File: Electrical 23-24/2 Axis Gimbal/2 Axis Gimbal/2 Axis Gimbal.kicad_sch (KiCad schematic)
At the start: 25 parts, among them IC1 BNO085, J1 Conn_01x06_Socket, U1 ATtiny404-SS

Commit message: Fix some gimbal problems
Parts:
- added I2C, Power: Conn_01x02_Socket, symbol Connector:Conn_01x02_Socket
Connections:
- net +BATT: now also Power.1 (Pin_1)
- net GND: now also Power.2 (Pin_2)
- net MOSI: now also U1.11 (PA1); no longer U1.13 (PA3)
- net RX: now also U1.6 (PB3); no longer U1.7 (PB2)
- net SCK: now also U1.13 (PA3); no longer U1.11 (PA1)
- net TX: now also U1.7 (PB2); no longer U1.6 (PB3)
- net SDA: now reaches U1.8 (PB1)
- net SDA: now also I2C.1 (Pin_1)
- net SCL: now reaches U1.9 (PB0)
- net SCL: now also I2C.2 (Pin_2)
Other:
- note added: "I2C Breakout"
- note added: "Power"
- moved on the sheet: C2, C3, D-CUP, D-CUP1, D-CUP2, IC1, R1, R2, R3, R4, R5, R6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

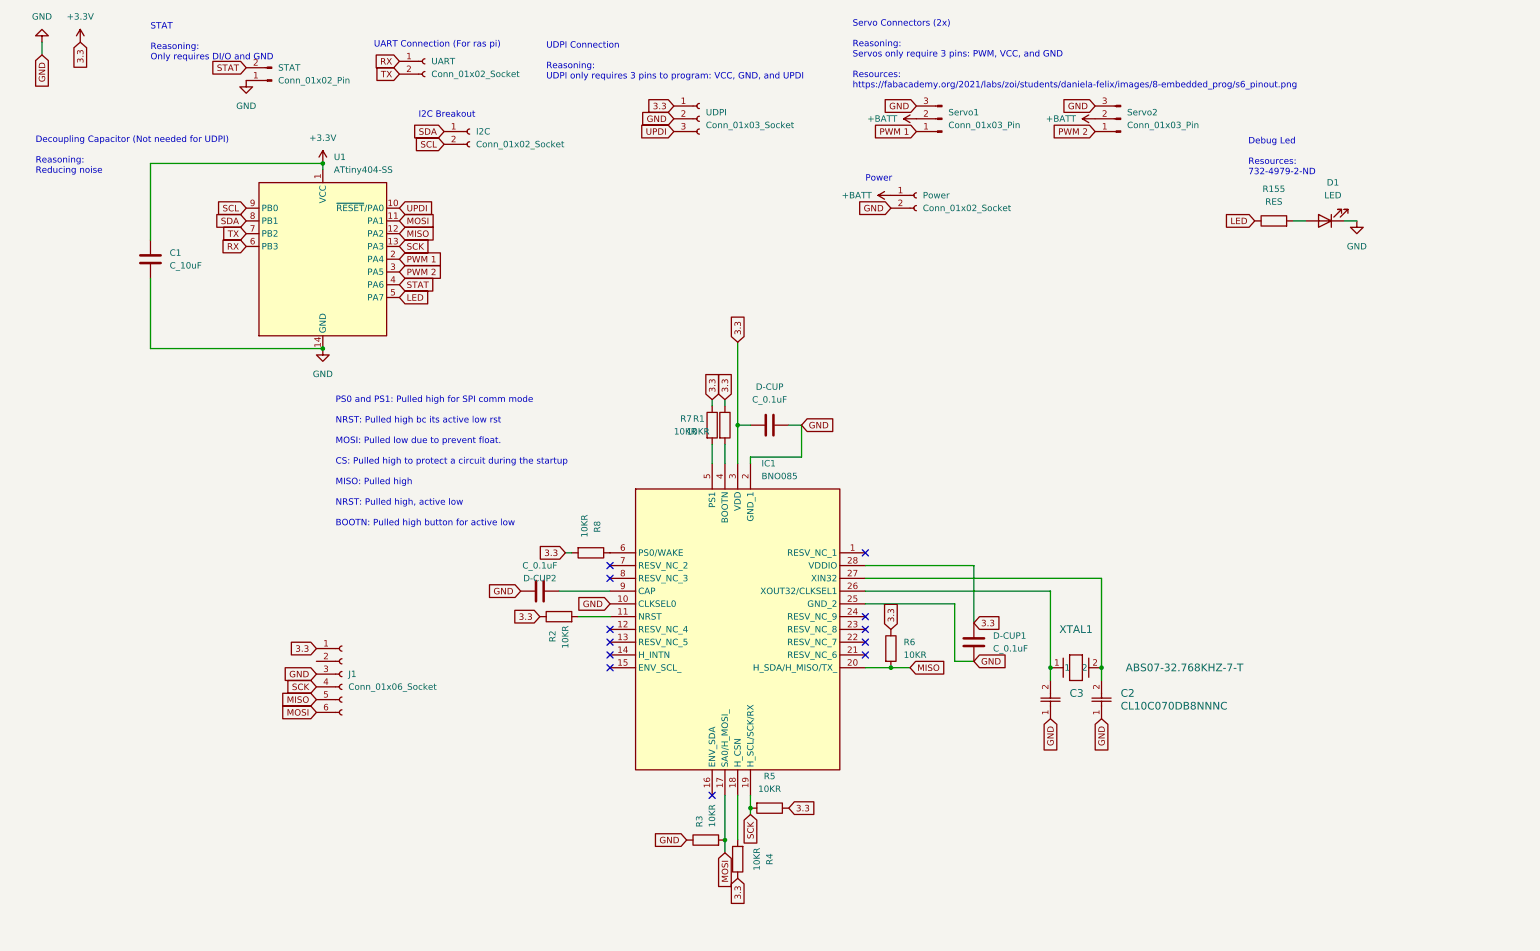
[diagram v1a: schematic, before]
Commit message: Added I2C
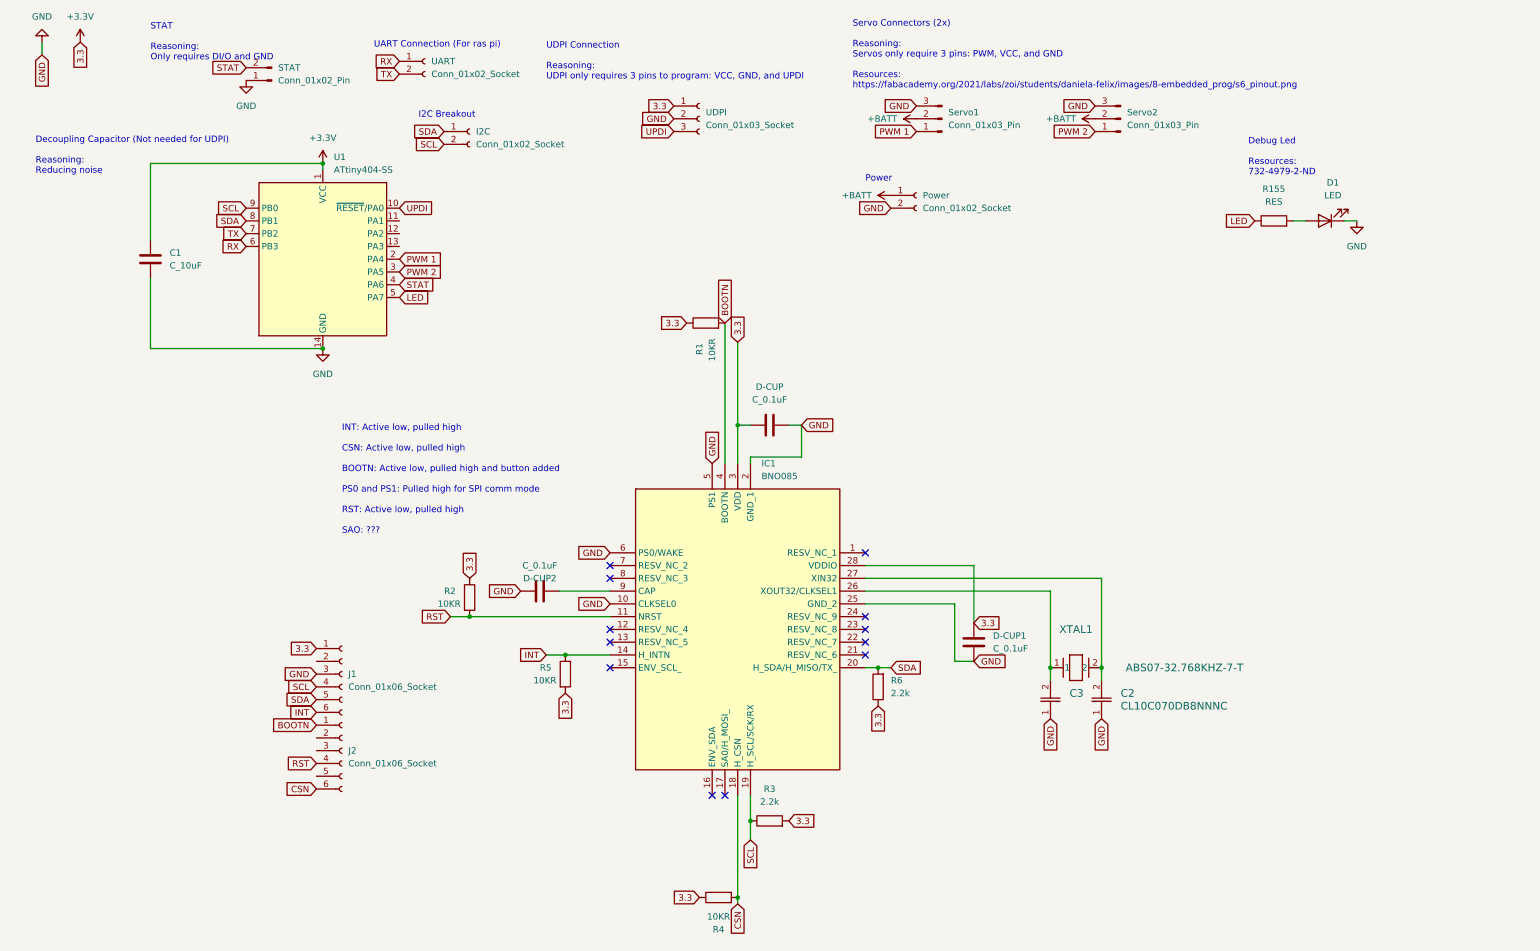
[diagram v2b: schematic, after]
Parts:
- removed R3, R6, R7, R8: 10KR, symbol oem:10KR
- added J2: Conn_01x06_Socket, symbol Connector:Conn_01x06_Socket
- added R3, R6: 2.2k, symbol Device:R
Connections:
- net +3.3V: now also R5.2, R3.2, R6.1; no longer R5.1
- net GND: now also IC1.5 (PS1), IC1.6 (PS0/WAKE)
- net SCL: now also IC1.19 (H_SCL/SCK/RX), J1.4 (Pin_4), R3.1
- net SDA: now also IC1.20 (H_SDA/H_MISO/TX_), J1.5 (Pin_5), R6.2
- net RST: now reaches IC1.11 (NRST), R2.2
- net RST: now also J2.4 (Pin_4)
- net INT: now reaches IC1.14 (H_INTN)
- net INT: now also J1.6 (Pin_6), R5.1
- net CSN: now reaches IC1.18 (H_CSN), R4.2
- net CSN: now also J2.6 (Pin_6)
- net BOOTN: now reaches IC1.4 (BOOTN), R1.2
- net BOOTN: now also J2.1 (Pin_1)
- removed net MISO: IC1.20 (H_SDA/H_MISO/TX_), J1.5 (Pin_5), U1.12 (PA2)
- removed net MOSI: IC1.17 (SA0/H_MOSI_), J1.6 (Pin_6), U1.11 (PA1)
- removed net SCK: IC1.19 (H_SCL/SCK/RX), J1.4 (Pin_4), R5.2, U1.13 (PA3)
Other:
- note added: "INT: Active low, pulled high CSN: Active low, pulled high BOOTN: Active low, pulled high and button added PS0 and PS1: Pulled high for SPI comm mode RST: Active low, pulled high SAO: ???"
- note removed: "PS0 and PS1: Pulled high for SPI comm mode NRST: Pulled high bc its active low rst MOSI: Pulled low due to prevent float. CS: Pulled high to protect a circuit during the startup MISO: Pulled high NRST: Pulled high, active low BOOTN: Pulled high button for active low"
- moved on the sheet: R1, R2, R4

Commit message: Finished Final Schematic
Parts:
- added C4, C5: C_100uF, Capacitor_SMD:C_1206_3216Metric_Pad1.33x1.80mm_HandSolder, symbol formula:C_100uF
- added IC2: AP1086DL-13, TO252-3L_1, symbol VReg3.3:AP1086DL-13
- C1: footprint footprints:C_0805_OEM -> Capacitor_SMD:C_0805_2012Metric_Pad1.18x1.45mm_HandSolder
- C2, C3: footprint CAP_CL10_SAM -> Capacitor_SMD:C_0201_0603Metric_Pad0.64x0.40mm_HandSolder
- D-CUP, D-CUP1, D-CUP2: footprint footprints:C_0805_OEM -> Capacitor_SMD:C_0402_1005Metric_Pad0.74x0.62mm_HandSolder
- D1: footprint (none) -> LED_SMD:LED_0603_1608Metric_Pad1.05x0.95mm_HandSolder
- I2C, Power, UART: footprint (none) -> Connector_PinSocket_2.54mm:PinSocket_1x02_P2.54mm_Vertical
- J1, J2: footprint (none) -> Connector_PinHeader_2.54mm:PinHeader_1x06_P2.54mm_Vertical
- R1: footprint (none) -> Resistor_SMD:R_0201_0603Metric_Pad0.64x0.40mm_HandSolder
- R2, R4, R5: footprint (none) -> Resistor_SMD:R_0603_1608Metric_Pad0.98x0.95mm_HandSolder
- R3, R6: footprint (none) -> Resistor_SMD:R_1206_3216Metric_Pad1.30x1.75mm_HandSolder
- R55: renamed from R155; footprint (none) -> LED_SMD:LED_1206_3216Metric_Pad1.42x1.75mm_HandSolder
- STAT: footprint (none) -> Connector_PinHeader_2.54mm:PinHeader_1x02_P2.54mm_Vertical
- Servo1, Servo2: footprint (none) -> Connector_PinHeader_2.54mm:PinHeader_1x03_P2.54mm_Vertical
- UDPI: footprint (none) -> Connector_PinSocket_2.54mm:PinSocket_1x03_P2.54mm_Vertical
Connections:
- net GND: now also C4.2, C5.2, IC2.1 (ADJ_(GND))
- net +3.3V renamed 3.3
- net 3.3: now also C4.1, IC2.3 (VOUT)
- new net +5V: C5.1, IC2.2 (VIN)
- no-connect marks 12 -> 19
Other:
- moved on the sheet: J1, J2

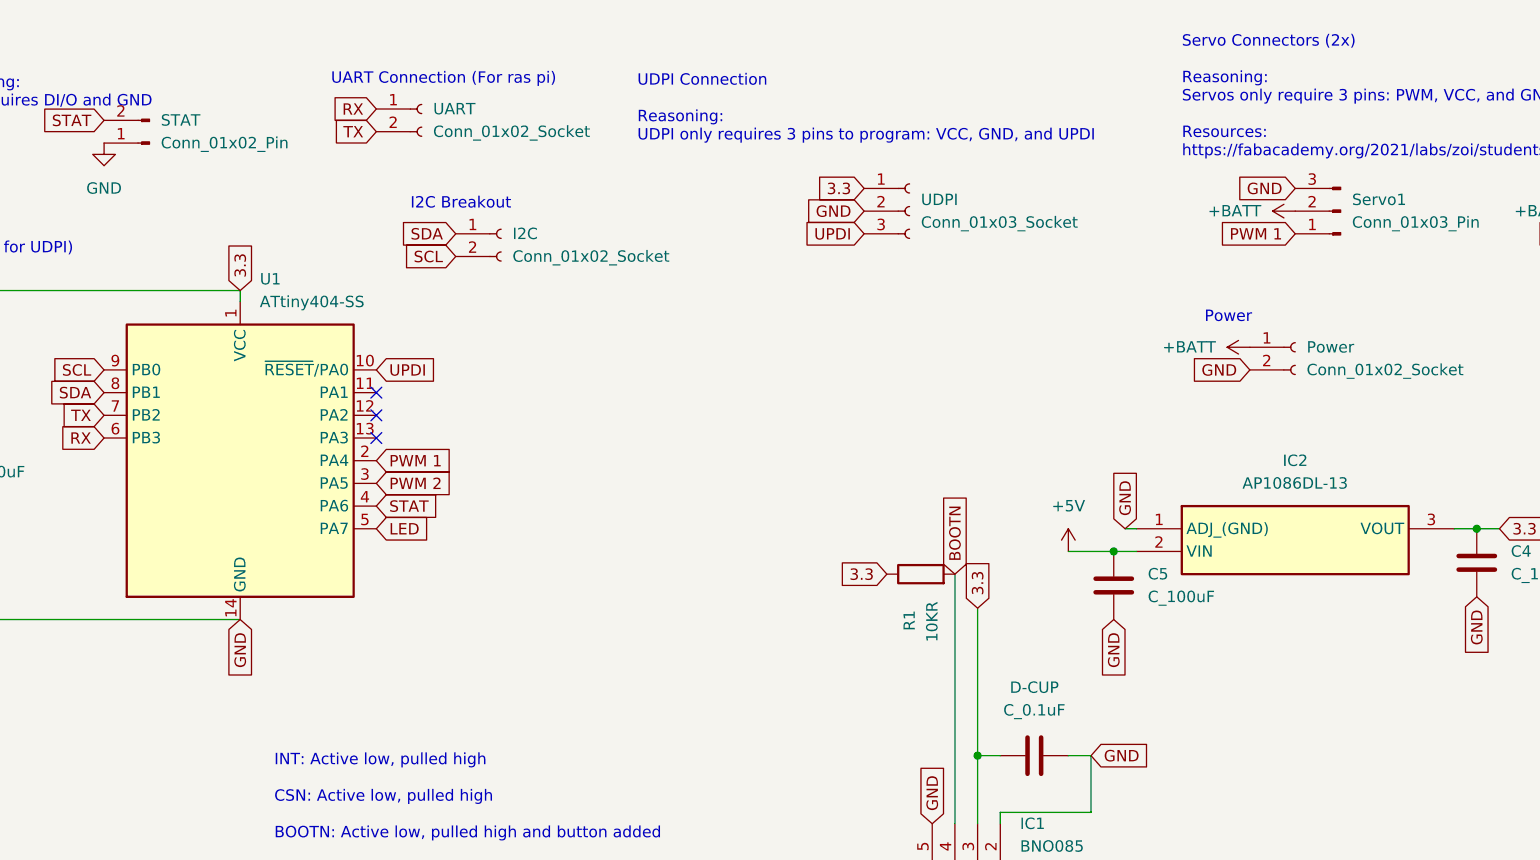
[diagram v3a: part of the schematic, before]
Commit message: Added Footprints
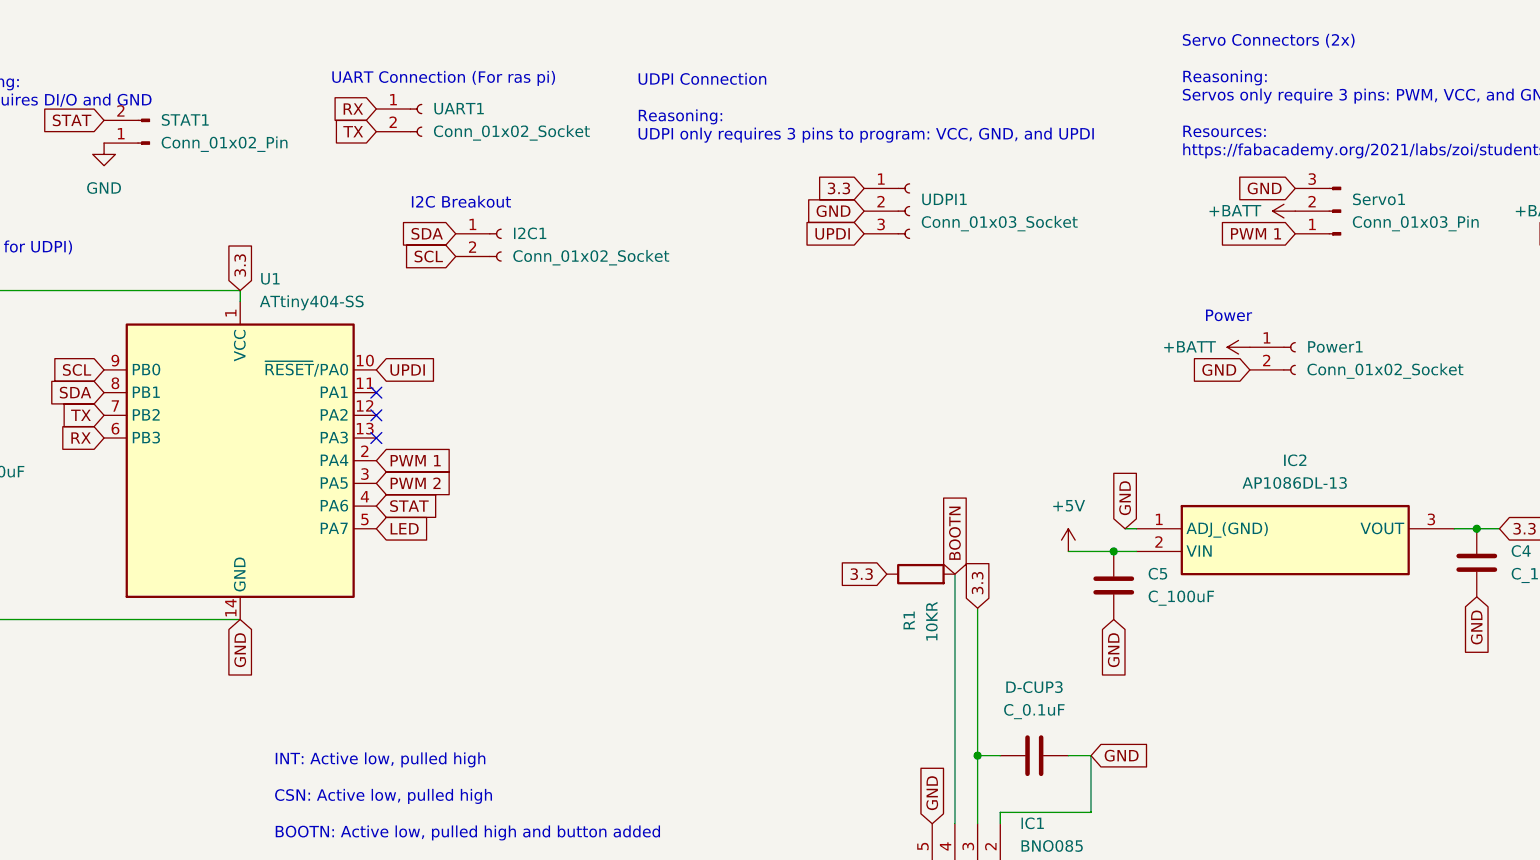
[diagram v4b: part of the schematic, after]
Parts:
- IC1: footprint BNO085 -> BNO085:BNO085
- IC2: footprint TO252-3L_1 -> VReg3.3:TO252-3L_1
- XTAL1: footprint XTAL_ABS07-32.768KHZ-7-T_ABR -> 32Crys:XTAL_ABS07-32.768KHZ-7-T_ABR
- renumbered D-CUP to D-CUP3, I2C to I2C1, Power to Power1, STAT to STAT1, UART to UART1, UDPI to UDPI1
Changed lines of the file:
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@@
   (symbol (lib_id "Connector:Conn_01x02_Pin") (at 63.5 26.67 180) (unit 1)
     (in_bom yes) (on_board yes) (dnp no) (fields_autoplaced)
-    (property "Reference" "STAT" (at 64.77 24.13 0)
+    (property "Reference" "STAT1" (at 64.77 24.13 0)
       (effects (font (size 1.27 1.27)) (justify right))
     )
@@
       (project "2 Axis Gimbal"
         (path "/b10b2b59-31cc-4d60-bc5f-41542c343df0"
-          (reference "STAT") (unit 1)
+          (reference "STAT1") (unit 1)
         )
       )
@@
   (symbol (lib_id "Connector:Conn_01x02_Socket") (at 191.77 49.53 0) (unit 1)
     (in_bom yes) (on_board yes) (dnp no) (fields_autoplaced)
-    (property "Reference" "Power" (at 193.04 49.53 0)
+    (property "Reference" "Power1" (at 193.04 49.53 0)
       (effects (font (size 1.27 1.27)) (justify left))
     )
@@
       (project "2 Axis Gimbal"
         (path "/b10b2b59-31cc-4d60-bc5f-41542c343df0"
-          (reference "Power") (unit 1)
+          (reference "Power1") (unit 1)
         )
       )
@@
       (effects (font (size 1.27 1.27)) (justify left))
     )
-    (property "Footprint" "BNO085" (at 177.8 205.41 0)
+    (property "Footprint" "BNO085:BNO085" (at 177.8 205.41 0)
       (effects (font (size 1.27 1.27)) (justify left top) hide)
     )
@@
   (symbol (lib_id "Connector:Conn_01x02_Socket") (at 93.98 22.86 0) (unit 1)
     (in_bom yes) (on_board yes) (dnp no) (fields_autoplaced)
-    (property "Reference" "UART" (at 95.25 22.86 0)
+    (property "Reference" "UART1" (at 95.25 22.86 0)
       (effects (font (size 1.27 1.27)) (justify left))
     )
@@
       (project "2 Axis Gimbal"
         (path "/b10b2b59-31cc-4d60-bc5f-41542c343df0"
-          (reference "UART") (unit 1)
+          (reference "UART1") (unit 1)
         )
       )
@@
   (symbol (lib_id "formula:C_0.1uF") (at 162.56 95.25 90) (unit 1)
     (in_bom yes) (on_board yes) (dnp no) (fields_autoplaced)
-    (property "Reference" "D-CUP" (at 162.56 87.63 90)
+    (property "Reference" "D-CUP3" (at 162.56 87.63 90)
       (effects (font (size 1.27 1.27)))
     )
@@
       (project "2 Axis Gimbal"
         (path "/b10b2b59-31cc-4d60-bc5f-41542c343df0"
-          (reference "D-CUP") (unit 1)
+          (reference "D-CUP3") (unit 1)
         )
       )
@@
       (effects (font (size 1.524 1.524)))
     )
-    (property "Footprint" "XTAL_ABS07-32.768KHZ-7-T_ABR" (at 218.44 143.51 0)
+    (property "Footprint" "32Crys:XTAL_ABS07-32.768KHZ-7-T_ABR" (at 218.44 143.51 0)
       (effects (font (size 1.27 1.27) italic) hide)
     )
@@
   (symbol (lib_id "Connector:Conn_01x02_Socket") (at 102.87 36.83 0) (unit 1)
     (in_bom yes) (on_board yes) (dnp no) (fields_autoplaced)
-    (property "Reference" "I2C" (at 104.14 36.83 0)
+    (property "Reference" "I2C1" (at 104.14 36.83 0)
       (effects (font (size 1.27 1.27)) (justify left))
     )
@@
       (project "2 Axis Gimbal"
         (path "/b10b2b59-31cc-4d60-bc5f-41542c343df0"
-          (reference "I2C") (unit 1)
+          (reference "I2C1") (unit 1)
         )
       )
@@
   (symbol (lib_id "Connector:Conn_01x03_Socket") (at 148.59 34.29 0) (unit 1)
     (in_bom yes) (on_board yes) (dnp no) (fields_autoplaced)
-    (property "Reference" "UDPI" (at 149.86 33.02 0)
+    (property "Reference" "UDPI1" (at 149.86 33.02 0)
       (effects (font (size 1.27 1.27)) (justify left))
     )
@@
       (project "2 Axis Gimbal"
         (path "/b10b2b59-31cc-4d60-bc5f-41542c343df0"
-          (reference "UDPI") (unit 1)
+          (reference "UDPI1") (unit 1)
         )
       )
@@
       (effects (font (size 1.27 1.27)))
     )
-    (property "Footprint" "TO252-3L_1" (at 205.74 164.77 0)
+    (property "Footprint" "VReg3.3:TO252-3L_1" (at 205.74 164.77 0)
       (effects (font (size 1.27 1.27)) (justify left top) hide)
     )

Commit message: Starteddddd
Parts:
- removed I2C1: Conn_01x02_Socket, Connector_PinSocket_2.54mm:PinSocket_1x02_P2.54mm_Vertical, symbol Connector:Conn_01x02_Socket
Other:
- note removed: "I2C Breakout"
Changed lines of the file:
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@@
-    (effects (font (size 1.27 1.27)) (justify left bottom))
-  )
-  (text "I2C Breakout" (at 92.71 34.29 0)
     (effects (font (size 1.27 1.27)) (justify left bottom))
   )
@@
     )
   )
-  (global_label "SCL" (shape input) (at 97.79 39.37 180) (fields_autoplaced)
-    (effects (font (size 1.27 1.27)) (justify right))
-    (property "Intersheetrefs" "${INTERSHEET_REFS}" (at 91.2972 39.37 0)
-      (effects (font (size 1.27 1.27)) (justify right) hide)
-    )
-  )
   (global_label "GND" (shape input) (at 143.51 34.29 180) (fields_autoplaced)
     (effects (font (size 1.27 1.27)) (justify right))
@@
     (effects (font (size 1.27 1.27)) (justify right))
     (property "Intersheetrefs" "${INTERSHEET_REFS}" (at 217.9949 36.83 0)
-      (effects (font (size 1.27 1.27)) (justify right) hide)
-    )
-  )
-  (global_label "SDA" (shape input) (at 97.79 36.83 180) (fields_autoplaced)
-    (effects (font (size 1.27 1.27)) (justify right))
-    (property "Intersheetrefs" "${INTERSHEET_REFS}" (at 91.2367 36.83 0)
       (effects (font (size 1.27 1.27)) (justify right) hide)
     )
@@
         )
       )
-    )
-  )
-  (symbol (lib_id "Connector:Conn_01x02_Socket") (at 102.87 36.83 0) (unit 1)
-    (in_bom yes) (on_board yes) (dnp no) (fields_autoplaced)
-    (property "Reference" "I2C1" (at 104.14 36.83 0)
-      (effects (font (size 1.27 1.27)) (justify left))
-    )
-    (property "Value" "Conn_01x02_Socket" (at 104.14 39.37 0)
-      (effects (font (size 1.27 1.27)) (justify left))
-    )
-    (property "Footprint" "Connector_PinSocket_2.54mm:PinSocket_1x02_P2.54mm_Vertical" (at 102.87 36.83 0)
-      (effects (font (size 1.27 1.27)) hide)
-    )
-    (property "Datasheet" "~" (at 102.87 36.83 0)
-      (effects (font (size 1.27 1.27)) hide)
-    )
-    (pin "1")
-    (pin "2")
-    (instances
-      (project "2 Axis Gimbal"
-        (path "/b10b2b59-31cc-4d60-bc5f-41542c343df0"
-          (reference "I2C1") (unit 1)
-        )
-      )
